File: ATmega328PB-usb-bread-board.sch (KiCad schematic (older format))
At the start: 32 parts, among them J1 Conn_01x17, J2 Conn_01x17, J3 USB_B_Micro, J4 AVR-ISP-6, J5 Grove-I2C-connector, J6 Grove-I2C-connector, J7 Grove-I2C-connector, U1 ATmega328PB-MU, U2 CP2102N-A01-GQFN28, U3 LMV358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

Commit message: Remove jumper for AVCC
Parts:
- removed JP1: NC, my-kicad-footprints:SolderJumper-2_P1.3mm_Bridged_RoundedPad1.0x1.5mm, symbol ATmega328PB-usb-bread-board-rescue:Jumper_NC_Small-Device
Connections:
- net avcc is gone; now on net VCC: J2.16 (Pin_16), U1.18 (AVCC)
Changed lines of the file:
@@
 	1    0    0    -1
 $EndComp
-Wire Wire Line
-	5550 1200 5550 1500
 $Comp
 L power:GND #PWR0104
@@
 	1    0    0    -1
 $EndComp
-$Comp
-L ATmega328PB-usb-bread-board-rescue:Jumper_NC_Small-Device JP1
-U 1 1 5EF1D9B3
-P 5650 1500
-F 0 "JP1" H 5650 1712 50  0000 C CNN
-F 1 "NC" H 5650 1621 50  0000 C CNN
-F 2 "my-kicad-footprints:SolderJumper-2_P1.3mm_Bridged_RoundedPad1.0x1.5mm" H 5650 1500 50  0001 C CNN
-F 3 "~" H 5650 1500 50  0001 C CNN
-	1    5650 1500
-	1    0    0    -1
-$EndComp
-Connection ~ 5550 1500
-Wire Wire Line
-	5550 1500 5550 1750
-Wire Wire Line
-	5750 1500 5750 1650
-Wire Wire Line
-	5750 1650 5650 1650
-Wire Wire Line
-	5650 1650 5650 1750
 $Comp
 L power:GND #PWR0105
@@
 	1    0    0    -1
 $EndComp
-Text Label 8750 4300 0    50   ~ 0
-avcc
-Text Label 5750 1500 0    50   ~ 0
-avcc
 Wire Wire Line
 	5150 1200 5550 1200
@@
 Connection ~ 3700 1500
 $Comp
-L power:+3V3 #PWR?
+L power:+3V3 #PWR0111
 U 1 1 5F9873FD
 P 4050 1500
-F 0 "#PWR?" H 4050 1350 50  0001 C CNN
+F 0 "#PWR0111" H 4050 1350 50  0001 C CNN
 F 1 "+3V3" H 4065 1673 50  0000 C CNN
 F 2 "" H 4050 1500 50  0001 C CNN
@@
 Wire Wire Line
 	2850 1400 3350 1400
+Wire Wire Line
+	5550 1200 5550 1750
+Wire Wire Line
+	5650 1200 5550 1200
+Wire Wire Line
+	5650 1200 5650 1750
+$Comp
+L power:VCC #PWR?
+U 1 1 5F911877
+P 9000 4300
+F 0 "#PWR?" H 9000 4150 50  0001 C CNN
+F 1 "VCC" H 9015 4473 50  0000 C CNN
+F 2 "" H 9000 4300 50  0001 C CNN
+F 3 "" H 9000 4300 50  0001 C CNN
+	1    9000 4300
+	1    0    0    -1
+$EndComp
+Wire Wire Line
+	9000 4300 8750 4300
 $EndSCHEMATC

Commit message: Change zenar and change position of led and usb
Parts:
- removed JP3, JP4: NC, my-kicad-footprints:SolderJumper-2_P1.3mm_Bridged_RoundedPad1.0x1.5mm, symbol ATmega328PB-usb-bread-board-rescue:Jumper_NC_Small-Device
- D1, D2, D3: footprint my-kicad-footprints:D_UMD2 -> Diode_SMD:D_SOD-523
- R3: value 1k -> 10k
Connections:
- net pd0 is gone; now on net USB_UART_TX: J1.3 (Pin_3), U1.30 (PD0)
- net pd1 is gone; now on net USB_UART_RX: J1.2 (Pin_2), U1.31 (PD1)
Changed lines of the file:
@@
 F 0 "D3" V 2100 2900 50  0000 L CNN
 F 1 "DZ" V 2300 2900 50  0000 L CNN
-F 2 "my-kicad-footprints:D_UMD2" H 2200 2900 50  0001 C CNN
+F 2 "Diode_SMD:D_SOD-523" H 2200 2900 50  0001 C CNN
 F 3 "~" H 2200 2900 50  0001 C CNN
 	1    2200 2900
@@
 F 0 "D2" V 1950 2900 50  0000 L CNN
 F 1 "DZ" V 2150 2900 50  0000 L CNN
-F 2 "my-kicad-footprints:D_UMD2" H 2050 2900 50  0001 C CNN
+F 2 "Diode_SMD:D_SOD-523" H 2050 2900 50  0001 C CNN
 F 3 "~" H 2050 2900 50  0001 C CNN
 	1    2050 2900
@@
 F 0 "D1" V 1800 2900 50  0000 L CNN
 F 1 "DZ" V 2000 2900 50  0000 L CNN
-F 2 "my-kicad-footprints:D_UMD2" H 1900 2900 50  0001 C CNN
+F 2 "Diode_SMD:D_SOD-523" H 1900 2900 50  0001 C CNN
 F 3 "~" H 1900 2900 50  0001 C CNN
 	1    1900 2900
@@
 Wire Wire Line
 	8200 3100 7950 3100
-Wire Wire Line
-	6600 3750 6700 3750
-Wire Wire Line
-	6700 3850 6600 3850
 Text Label 6700 3850 0    50   ~ 0
 USB_UART_RX
 Text Label 6700 3750 0    50   ~ 0
 USB_UART_TX
-Wire Wire Line
-	6150 3750 6400 3750
-Wire Wire Line
-	6400 3850 6150 3850
-$Comp
-L ATmega328PB-usb-bread-board-rescue:Jumper_NC_Small-Device JP4
-U 1 1 5F5C0BDD
-P 6500 3850
-F 0 "JP4" H 6600 3900 50  0000 C CNN
-F 1 "NC" H 6400 3900 50  0000 C CNN
-F 2 "my-kicad-footprints:SolderJumper-2_P1.3mm_Bridged_RoundedPad1.0x1.5mm" H 6500 3850 50  0001 C CNN
-F 3 "~" H 6500 3850 50  0001 C CNN
-	1    6500 3850
-	1    0    0    -1
-$EndComp
-$Comp
-L ATmega328PB-usb-bread-board-rescue:Jumper_NC_Small-Device JP3
-U 1 1 5F5B8F20
-P 6500 3750
-F 0 "JP3" H 6600 3800 50  0000 C CNN
-F 1 "NC" H 6400 3800 50  0000 C CNN
-F 2 "my-kicad-footprints:SolderJumper-2_P1.3mm_Bridged_RoundedPad1.0x1.5mm" H 6500 3750 50  0001 C CNN
-F 3 "~" H 6500 3750 50  0001 C CNN
-	1    6500 3750
-	1    0    0    -1
-$EndComp
 Wire Wire Line
 	6350 3550 6150 3550
@@
 P 4700 6600
 F 0 "R3" H 4770 6646 50  0000 L CNN
-F 1 "1k" H 4770 6555 50  0000 L CNN
+F 1 "10k" H 4770 6555 50  0000 L CNN
 F 2 "Resistor_SMD:R_0603_1608Metric" V 4630 6600 50  0001 C CNN
 F 3 "~" H 4700 6600 50  0001 C CNN
@@
 	5650 1200 5650 1750
 $Comp
-L power:VCC #PWR?
+L power:VCC #PWR0124
 U 1 1 5F911877
 P 9000 4300
-F 0 "#PWR?" H 9000 4150 50  0001 C CNN
+F 0 "#PWR0124" H 9000 4150 50  0001 C CNN
 F 1 "VCC" H 9015 4473 50  0000 C CNN
 F 2 "" H 9000 4300 50  0001 C CNN
@@
 Wire Wire Line
 	9000 4300 8750 4300
+Wire Wire Line
+	6700 3750 6150 3750
+Wire Wire Line
+	6150 3850 6700 3850
 $EndSCHEMATC

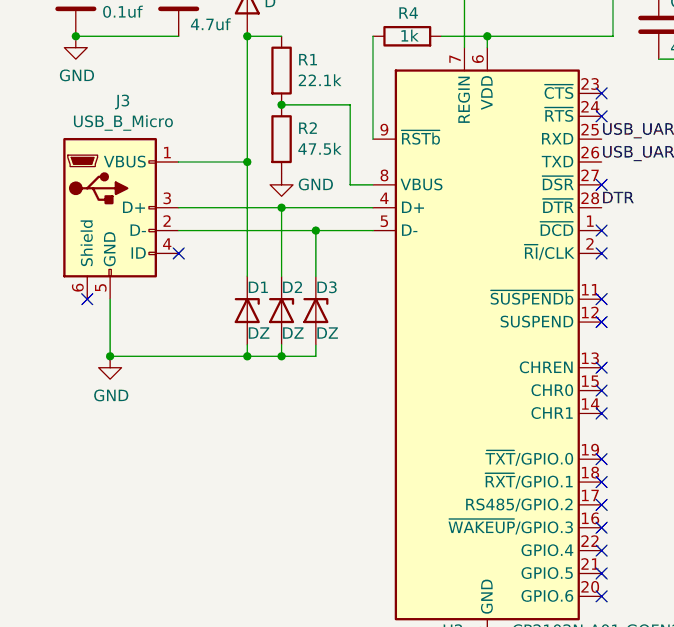
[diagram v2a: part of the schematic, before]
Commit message: Use diode array and update holes position as Rev2021.03
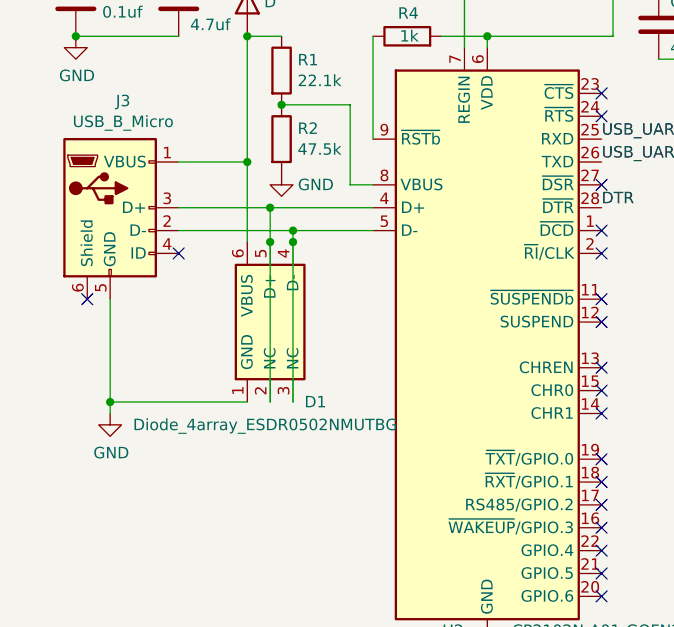
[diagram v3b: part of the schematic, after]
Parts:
- removed D1, D2, D3: DZ, Diode_SMD:D_SOD-523, symbol Device:D_Zener
- added D1: Diode_4array_ESDR0502NMUTBG, my-kicad-footprints:OnSemi_UDFN-6_1.2x1.0mm_P0.4mm, symbol my-kicad-symbols:Diode_4array_ESDR0502NMUTBG
- C1, C2, C3, C4, C7, C9: footprint Capacitor_SMD:C_0603_1608Metric -> Capacitor_SMD:C_0402_1005Metric
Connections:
- net GND: now also D1.1 (GND)
- net at J3.3 (D+), U2.4 (D+): now also D1.2 (NC), D1.5 (D+)
- net at J3.2 (D-), U2.5 (D-): now also D1.3 (NC), D1.4 (D-)
- net at D5.2 (A), J3.1 (VBUS), R1.1: now also D1.6 (VBUS)
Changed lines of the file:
@@
 F 0 "C1" H 4815 2246 50  0000 L CNN
 F 1 "0.1uf" H 4815 2155 50  0000 L CNN
-F 2 "Capacitor_SMD:C_0603_1608Metric" H 4738 2050 50  0001 C CNN
+F 2 "Capacitor_SMD:C_0402_1005Metric" H 4738 2050 50  0001 C CNN
 F 3 "~" H 4700 2200 50  0001 C CNN
 	1    4700 2200
@@
 F 0 "C2" H 5265 1396 50  0000 L CNN
 F 1 "0.1uf" H 5265 1305 50  0000 L CNN
-F 2 "Capacitor_SMD:C_0603_1608Metric" H 5188 1200 50  0001 C CNN
+F 2 "Capacitor_SMD:C_0402_1005Metric" H 5188 1200 50  0001 C CNN
 F 3 "~" H 5150 1350 50  0001 C CNN
 	1    5150 1350
@@
 L power:GND #PWR0109
 U 1 1 5F591B17
-P 1300 3100
-F 0 "#PWR0109" H 1300 2850 50  0001 C CNN
-F 1 "GND" H 1305 2927 50  0000 C CNN
-F 2 "" H 1300 3100 50  0001 C CNN
-F 3 "" H 1300 3100 50  0001 C CNN
-	1    1300 3100
-	1    0    0    -1
-$EndComp
-$Comp
-L Device:D_Zener D3
-U 1 1 5F592324
-P 2200 2900
-F 0 "D3" V 2100 2900 50  0000 L CNN
-F 1 "DZ" V 2300 2900 50  0000 L CNN
-F 2 "Diode_SMD:D_SOD-523" H 2200 2900 50  0001 C CNN
-F 3 "~" H 2200 2900 50  0001 C CNN
-	1    2200 2900
-	0    1    1    0
-$EndComp
-$Comp
-L Device:D_Zener D2
-U 1 1 5F592ED3
-P 2050 2900
-F 0 "D2" V 1950 2900 50  0000 L CNN
-F 1 "DZ" V 2150 2900 50  0000 L CNN
-F 2 "Diode_SMD:D_SOD-523" H 2050 2900 50  0001 C CNN
-F 3 "~" H 2050 2900 50  0001 C CNN
-	1    2050 2900
-	0    1    1    0
-$EndComp
-$Comp
-L Device:D_Zener D1
-U 1 1 5F593057
-P 1900 2900
-F 0 "D1" V 1800 2900 50  0000 L CNN
-F 1 "DZ" V 2000 2900 50  0000 L CNN
-F 2 "Diode_SMD:D_SOD-523" H 1900 2900 50  0001 C CNN
-F 3 "~" H 1900 2900 50  0001 C CNN
-	1    1900 2900
-	0    1    1    0
-$EndComp
-Wire Wire Line
-	1300 3100 1300 2850
-Wire Wire Line
-	2200 3050 2200 3100
-Wire Wire Line
-	2200 3100 2050 3100
-Connection ~ 1300 3100
-Wire Wire Line
-	1900 3100 1900 3050
-Connection ~ 1900 3100
-Wire Wire Line
-	1900 3100 1300 3100
-Wire Wire Line
-	2050 3050 2050 3100
-Connection ~ 2050 3100
-Wire Wire Line
-	2050 3100 1900 3100
-Wire Wire Line
-	2450 2450 2050 2450
-Wire Wire Line
-	1600 2550 2200 2550
-Wire Wire Line
-	2200 2750 2200 2550
-Connection ~ 2200 2550
-Wire Wire Line
-	2200 2550 2450 2550
-Wire Wire Line
-	2050 2750 2050 2450
-Connection ~ 2050 2450
-Wire Wire Line
-	2050 2450 1600 2450
-Wire Wire Line
-	1900 2750 1900 2250
+P 1300 3350
+F 0 "#PWR0109" H 1300 3100 50  0001 C CNN
+F 1 "GND" H 1305 3177 50  0000 C CNN
+F 2 "" H 1300 3350 50  0001 C CNN
+F 3 "" H 1300 3350 50  0001 C CNN
+	1    1300 3350
+	1    0    0    -1
+$EndComp
 Wire Wire Line
 	1900 2250 1600 2250
@@
 F 0 "C3" V 6600 3600 50  0000 L CNN
 F 1 "0.1uf" V 6600 3300 50  0000 L CNN
-F 2 "Capacitor_SMD:C_0603_1608Metric" H 6538 3400 50  0001 C CNN
+F 2 "Capacitor_SMD:C_0402_1005Metric" H 6538 3400 50  0001 C CNN
 F 3 "~" H 6500 3550 50  0001 C CNN
 	1    6500 3550
@@
 F 0 "C9" H 9450 3350 50  0000 L CNN
 F 1 "0.1uf" H 9450 3100 50  0000 L CNN
-F 2 "Capacitor_SMD:C_0603_1608Metric" H 9438 3100 50  0001 C CNN
+F 2 "Capacitor_SMD:C_0402_1005Metric" H 9438 3100 50  0001 C CNN
 F 3 "~" H 9400 3250 50  0001 C CNN
 	1    9400 3250
@@
 F 0 "C4" H 1265 1596 50  0000 L CNN
 F 1 "0.1uf" H 1265 1505 50  0000 L CNN
-F 2 "Capacitor_SMD:C_0603_1608Metric" H 1188 1400 50  0001 C CNN
+F 2 "Capacitor_SMD:C_0402_1005Metric" H 1188 1400 50  0001 C CNN
 F 3 "~" H 1150 1550 50  0001 C CNN
 	1    1150 1550
@@
 	1    0    0    -1
 $EndComp
+Wire Wire Line
+	1600 1400 1150 1400
+Connection ~ 1600 1400
+$Comp
+L Device:C C6
+U 1 1 5F9065CD
+P 3700 1650
+F 0 "C6" H 3750 1750 50  0000 L CNN
+F 1 "4.7uf" H 3750 1550 50  0000 L CNN
+F 2 "Capacitor_SMD:C_0402_1005Metric" H 3738 1500 50  0001 C CNN
+F 3 "~" H 3700 1650 50  0001 C CNN
+	1    3700 1650
+	1    0    0    -1
+$EndComp
+$Comp
+L Device:C C7
+U 1 1 5F906DB1
+P 4050 1650
+F 0 "C7" H 4165 1696 50  0000 L CNN
+F 1 "0.1uf" H 4165 1605 50  0000 L CNN
+F 2 "Capacitor_SMD:C_0402_1005Metric" H 4088 1500 50  0001 C CNN
+F 3 "~" H 4050 1650 50  0001 C CNN
+	1    4050 1650
+	1    0    0    -1
+$EndComp
+$Comp
+L power:GND #PWR0130
+U 1 1 5F90741A
+P 4050 1800
+F 0 "#PWR0130" H 4050 1550 50  0001 C CNN
+F 1 "GND" H 4055 1627 50  0000 C CNN
+F 2 "" H 4050 1800 50  0001 C CNN
+F 3 "" H 4050 1800 50  0001 C CNN
+	1    4050 1800
+	1    0    0    -1
+$EndComp
+Wire Wire Line
+	4050 1800 3700 1800
+Connection ~ 4050 1800
+Wire Wire Line
+	2950 1700 3500 1700
+Wire Wire Line
+	3500 1700 3500 1500
+Connection ~ 2950 1700
+Wire Wire Line
+	3500 1500 3700 1500
+Wire Wire Line
+	3700 1500 4050 1500
+Connection ~ 3700 1500
+$Comp
+L power:+3V3 #PWR0111
+U 1 1 5F9873FD
+P 4050 1500
+F 0 "#PWR0111" H 4050 1350 50  0001 C CNN
+F 1 "+3V3" H 4065 1673 50  0000 C CNN
+F 2 "" H 4050 1500 50  0001 C CNN
+F 3 "" H 4050 1500 50  0001 C CNN
+	1    4050 1500
+	1    0    0    -1
+$EndComp
+Connection ~ 4050 1500
+Wire Wire Line
+	1900 2250 1900 1700
+Wire Wire Line
+	1900 1700 2050 1700
+Wire Wire Line
+	2350 2000 2050 2000
+Wire Wire Line
+	2350 2000 2350 2350
+Connection ~ 2050 2000
+Connection ~ 2850 1400
+Wire Wire Line
+	2850 1400 3350 1400
+Wire Wire Line
+	5550 1200 5550 1750
+Wire Wire Line
+	5650 1200 5550 1200
+Wire Wire Line
+	5650 1200 5650 1750
+$Comp
+L power:VCC #PWR0124
+U 1 1 5F911877
+P 9000 4300
+F 0 "#PWR0124" H 9000 4150 50  0001 C CNN
+F 1 "VCC" H 9015 4473 50  0000 C CNN
+F 2 "" H 9000 4300 50  0001 C CNN
+F 3 "" H 9000 4300 50  0001 C CNN
+	1    9000 4300
+	1    0    0    -1
+$EndComp
+Wire Wire Line
+	9000 4300 8750 4300
+Wire Wire Line
+	6700 3750 6150 3750
+Wire Wire Line
+	6150 3850 6700 3850
+$Comp
+L my-kicad-symbols:Diode_4array_ESDR0502NMUTBG D1
+U 1 1 604D452D
+P 2000 2950
+F 0 "D1" V 1650 2800 50  0000 R CNN
+F 1 "Diode_4array_ESDR0502NMUTBG" V 1550 3550 50  0000 R CNN
+F 2 "my-kicad-footprints:OnSemi_UDFN-6_1.2x1.0mm_P0.4mm" H 2000 2950 50  0001 C CNN
+F 3 "" H 2000 2950 50  0001 C CNN
+	1    2000 2950
+	0    -1   -1   0
+$EndComp
+Connection ~ 1900 1700
+Wire Wire Line
+	1900 1400 2850 1400
+Wire Wire Line
+	1600 1400 1900 1400
+Connection ~ 1900 1400
 $Comp
 L Device:D D5
@@
 $EndComp
 Wire Wire Line
-	1600 1400 1150 1400
-Connection ~ 1600 1400
-$Comp
-L Device:C C6
-U 1 1 5F9065CD
-P 3700 1650
-F 0 "C6" H 3750 1750 50  0000 L CNN
-F 1 "4.7uf" H 3750 1550 50  0000 L CNN
-F 2 "Capacitor_SMD:C_0402_1005Metric" H 3738 1500 50  0001 C CNN
-F 3 "~" H 3700 1650 50  0001 C CNN
-	1    3700 1650
-	1    0    0    -1
-$EndComp
-$Comp
-L Device:C C7
-U 1 1 5F906DB1
-P 4050 1650
-F 0 "C7" H 4165 1696 50  0000 L CNN
-F 1 "0.1uf" H 4165 1605 50  0000 L CNN
-F 2 "Capacitor_SMD:C_0603_1608Metric" H 4088 1500 50  0001 C CNN
-F 3 "~" H 4050 1650 50  0001 C CNN
-	1    4050 1650
-	1    0    0    -1
-$EndComp
-$Comp
-L power:GND #PWR0130
-U 1 1 5F90741A
-P 4050 1800
-F 0 "#PWR0130" H 4050 1550 50  0001 C CNN
-F 1 "GND" H 4055 1627 50  0000 C CNN
-F 2 "" H 4050 1800 50  0001 C CNN
-F 3 "" H 4050 1800 50  0001 C CNN
-	1    4050 1800
-	1    0    0    -1
-$EndComp
-Wire Wire Line
-	4050 1800 3700 1800
-Connection ~ 4050 1800
-Wire Wire Line
-	2950 1700 3500 1700
-Wire Wire Line
-	3500 1700 3500 1500
-Connection ~ 2950 1700
-Wire Wire Line
-	3500 1500 3700 1500
-Wire Wire Line
-	3700 1500 4050 1500
-Connection ~ 3700 1500
-$Comp
-L power:+3V3 #PWR0111
-U 1 1 5F9873FD
-P 4050 1500
-F 0 "#PWR0111" H 4050 1350 50  0001 C CNN
-F 1 "+3V3" H 4065 1673 50  0000 C CNN
-F 2 "" H 4050 1500 50  0001 C CNN
-F 3 "" H 4050 1500 50  0001 C CNN
-	1    4050 1500
-	1    0    0    -1
-$EndComp
-Connection ~ 4050 1500
-Wire Wire Line
-	1600 1400 1900 1400
-Connection ~ 1900 1400
-Wire Wire Line
-	1900 2250 1900 1700
+	1600 2550 2100 2550
+Wire Wire Line
+	1600 2450 2000 2450
+Wire Wire Line
+	2100 2600 2100 2550
+Connection ~ 2100 2550
+Wire Wire Line
+	2100 2550 2450 2550
+Wire Wire Line
+	2000 2600 2000 2450
+Connection ~ 2000 2450
+Wire Wire Line
+	2000 2450 2450 2450
+Wire Wire Line
+	1900 2600 1900 2250
 Connection ~ 1900 2250
 Wire Wire Line
-	1900 1700 2050 1700
-Connection ~ 1900 1700
-Wire Wire Line
-	2350 2000 2050 2000
-Wire Wire Line
-	2350 2000 2350 2350
-Connection ~ 2050 2000
-Wire Wire Line
-	1900 1400 2850 1400
-Connection ~ 2850 1400
-Wire Wire Line
-	2850 1400 3350 1400
-Wire Wire Line
-	5550 1200 5550 1750
-Wire Wire Line
-	5650 1200 5550 1200
-Wire Wire Line
-	5650 1200 5650 1750
-$Comp
-L power:VCC #PWR0124
-U 1 1 5F911877
-P 9000 4300
-F 0 "#PWR0124" H 9000 4150 50  0001 C CNN
-F 1 "VCC" H 9015 4473 50  0000 C CNN
-F 2 "" H 9000 4300 50  0001 C CNN
-F 3 "" H 9000 4300 50  0001 C CNN
-	1    9000 4300
-	1    0    0    -1
-$EndComp
-Wire Wire Line
-	9000 4300 8750 4300
-Wire Wire Line
-	6700 3750 6150 3750
-Wire Wire Line
-	6150 3850 6700 3850
+	1300 2850 1300 3300
+Wire Wire Line
+	1300 3300 1900 3300
+Connection ~ 1300 3300
+Wire Wire Line
+	1300 3300 1300 3350
+Connection ~ 2100 2600
+Wire Wire Line
+	2100 2600 2100 3300
+Wire Wire Line
+	2000 3300 2000 2600
+Connection ~ 2000 2600
 $EndSCHEMATC

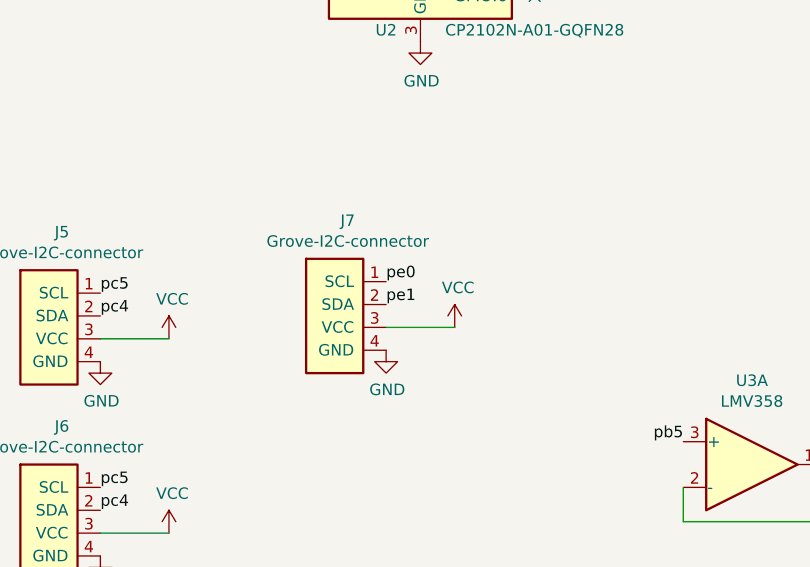
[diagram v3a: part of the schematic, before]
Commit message: Correct pin asign for Wire1 grove connector
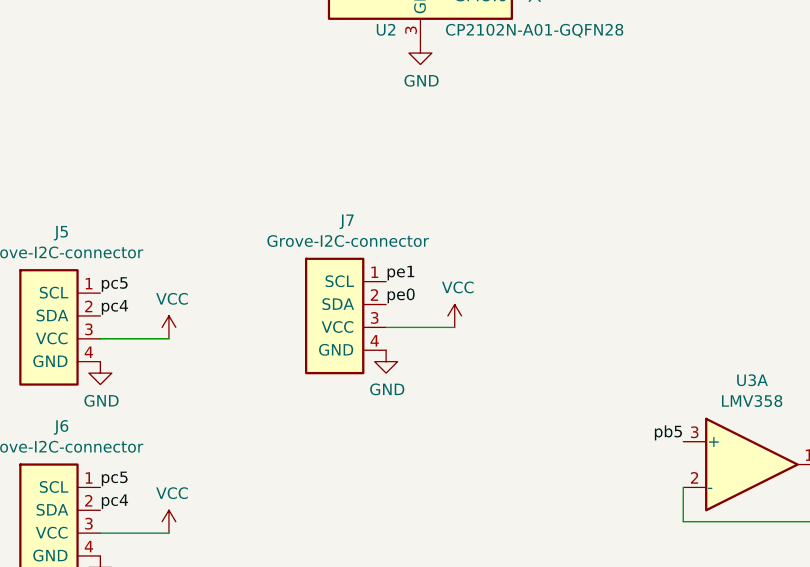
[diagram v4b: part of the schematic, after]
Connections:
- net pe0: now also J7.2 (SDA); no longer J7.1 (SCL)
- net pe1: now also J7.1 (SCL); no longer J7.2 (SDA)
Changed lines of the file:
@@
 Wire Wire Line
 	3100 5600 2800 5600
+Text Label 2800 5400 0    50   ~ 0
+pe1
 Text Label 2800 5500 0    50   ~ 0
-pe1
-Text Label 2800 5400 0    50   ~ 0
 pe0
 NoConn ~ 3450 2550

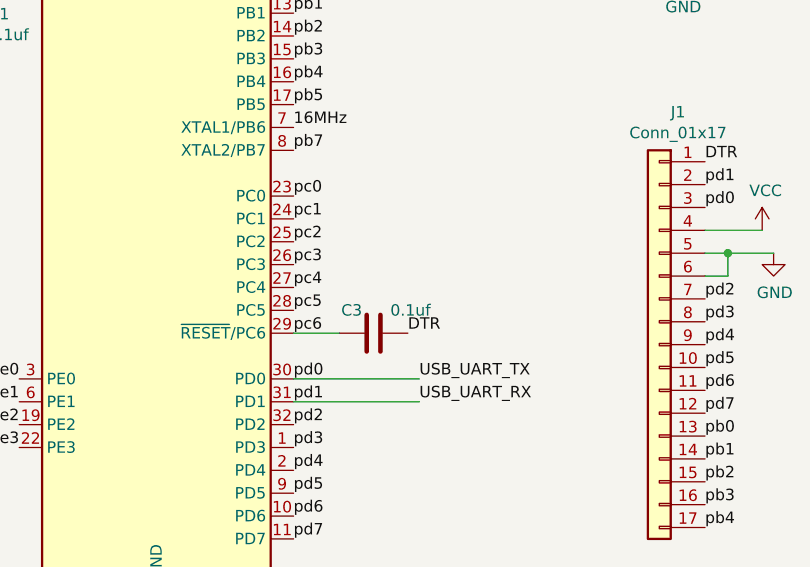
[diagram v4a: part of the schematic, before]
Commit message: Add pullup resistor to RST
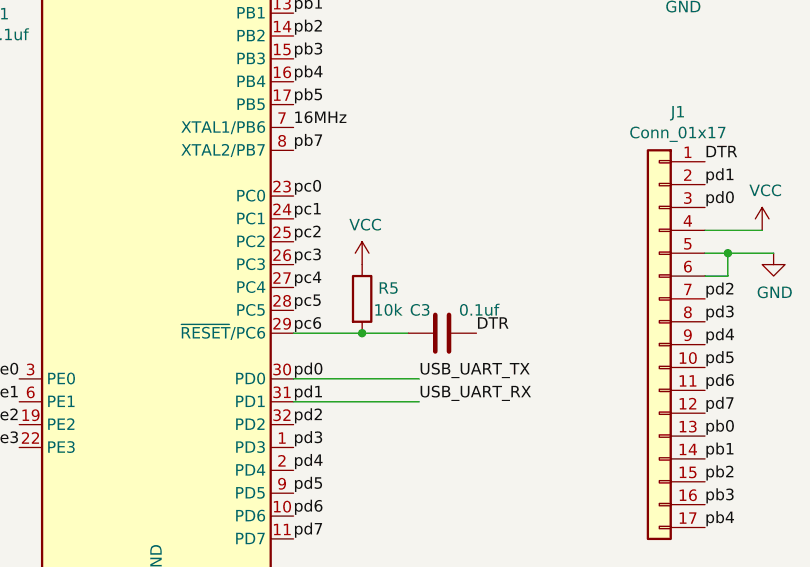
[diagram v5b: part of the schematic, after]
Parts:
- added R5: 10k, Resistor_SMD:R_0603_1608Metric, symbol Device:R
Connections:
- net VCC: now also R5.1
- net pc6: now also R5.2
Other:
- moved on the sheet: C3
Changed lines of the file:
@@
 L Device:C C3
 U 1 1 5F5C8013
-P 6500 3550
-F 0 "C3" V 6600 3600 50  0000 L CNN
-F 1 "0.1uf" V 6600 3300 50  0000 L CNN
-F 2 "Capacitor_SMD:C_0402_1005Metric" H 6538 3400 50  0001 C CNN
-F 3 "~" H 6500 3550 50  0001 C CNN
-	1    6500 3550
+P 6800 3550
+F 0 "C3" V 6900 3600 50  0000 L CNN
+F 1 "0.1uf" V 6900 3300 50  0000 L CNN
+F 2 "Capacitor_SMD:C_0402_1005Metric" H 6838 3400 50  0001 C CNN
+F 3 "~" H 6800 3550 50  0001 C CNN
+	1    6800 3550
 	0    -1   -1   0
 $EndComp
@@
 Text Label 6700 3750 0    50   ~ 0
 USB_UART_TX
-Wire Wire Line
-	6350 3550 6150 3550
-Text Label 6650 3550 0    50   ~ 0
+Text Label 6950 3550 0    50   ~ 0
 DTR
 Text Label 7950 2800 0    50   ~ 0
@@
 	2000 3300 2000 2600
 Connection ~ 2000 2600
+$Comp
+L Device:R R5
+U 1 1 60752C8B
+P 6450 3400
+F 0 "R5" H 6520 3446 50  0000 L CNN
+F 1 "10k" H 6500 3350 50  0000 L CNN
+F 2 "Resistor_SMD:R_0603_1608Metric" V 6380 3400 50  0001 C CNN
+F 3 "~" H 6450 3400 50  0001 C CNN
+	1    6450 3400
+	1    0    0    -1
+$EndComp
+Wire Wire Line
+	6150 3550 6450 3550
+Connection ~ 6450 3550
+Wire Wire Line
+	6450 3550 6650 3550
+$Comp
+L power:VCC #PWR0125
+U 1 1 60762B92
+P 6450 3250
+F 0 "#PWR0125" H 6450 3100 50  0001 C CNN
+F 1 "VCC" H 6465 3423 50  0000 C CNN
+F 2 "" H 6450 3250 50  0001 C CNN
+F 3 "" H 6450 3250 50  0001 C CNN
+	1    6450 3250
+	1    0    0    -1
+$EndComp
 $EndSCHEMATC
